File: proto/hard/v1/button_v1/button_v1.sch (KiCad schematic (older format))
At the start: 68 parts, among them J1 Conn_01x06_Female, J10 Conn_01x01_Female, J11 Conn_01x01_Female, J12 Conn_01x01_Female, J13 Conn_01x01_Female, J14 K3-2235D, J15 Conn_01x03_Male, J16 Conn_01x01_Male, J2 Conn_01x06_Female, J3 Conn_01x06_Female, J4 Conn_01x06_Female, J7 Conn_01x04_Female, J9 Conn_01x01_Female, Q1 TP0610T, Q3 TP0610T, Q6 UMG8N, Q7 UMG8N, Q8 IRLML2803, U1 LCD_2.8_SPI, U11 TC305, U12 LCD_1_8_SPI, U13 74HC595, U2 STM32F103C8Tx, U6 LM339, Y1 8MHz

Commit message: Finished main board PCB
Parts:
- removed J10, J11, J12, J13, J9: Conn_01x01_Female, Connector_Pin:Pin_D0.7mm_L6.5mm_W1.8mm_FlatFork, symbol Connector:Conn_01x01_Female
- removed J15: Conn_01x03_Male, Connector_PinHeader_2.54mm:PinHeader_1x03_P2.54mm_Vertical, symbol Connector:Conn_01x03_Male
- removed J16: Conn_01x01_Male, Connector_Pin:Pin_D0.7mm_L6.5mm_W1.8mm_FlatFork, symbol Connector:Conn_01x01_Male
- removed R35, R36, R37, R38: 3k, Resistor_SMD:R_0805_2012Metric_Pad1.15x1.40mm_HandSolder, symbol Device:R
- added J10: Conn_01x04_Male, Connector_PinHeader_2.54mm:PinHeader_1x04_P2.54mm_Vertical, symbol Connector:Conn_01x04_Male
- added J9: Conn_01x06_Male, brbuttonsystem:A1501WR-S-5P, symbol Connector:Conn_01x06_Male
- added R15: 47k, Resistor_SMD:R_0805_2012Metric_Pad1.15x1.40mm_HandSolder, symbol Device:R
- added RN2: 3k, Resistor_SMD:R_Array_Convex_4x0603, symbol Device:R_Pack04
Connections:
- net +3V3: now also R15.1
- net CX0: now also J9.1 (Pin_1)
- net CX1: now also J9.2 (Pin_2), RN2.4 (R4.1)
- net CX2: now also J9.3 (Pin_3), RN2.3 (R3.1)
- net CX3: now also J9.4 (Pin_4), RN2.2 (R2.1)
- net CX4: now also J9.5 (Pin_5), RN2.1 (R1.1)
- net EXTRA_TICK: now also U2.10 (PA0); no longer U2.41 (PB5)
- net GND: now also J10.2 (Pin_2), J9.6 (Pin_6)
- net LCD_CS: now also U2.3 (PC14); no longer U2.10 (PA0)
- net LCD_RESET: now also U12.2 (RESET)
- net MainLcdLed: now also Q8.1 (G), R12.2
- net NRST: now also J10.4 (Pin_4)
- net SWCLK: now also J10.1 (Pin_1)
- net SWDIO: now also J10.3 (Pin_3)
- net USB_PULLUP: now reaches U2.38 (PA15)
- net BACK_LCD_CS: now reaches U2.4 (PC15)
- net BACK_LCD_CS: now also U12.3 (CS)
- net at U11.5 (CX1): now also RN2.5 (R4.2)
- net at U11.6 (CX2): now also RN2.6 (R3.2)
- net at U11.7 (CX3): now also RN2.7 (R2.2)
- net at U11.8 (CX4): now also RN2.8 (R1.2)
- net at J14.3: now also R15.2
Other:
- note added: "MainLcdLed is used\nas a switch for front LCD\nand as a signal invertor\nfor back LCD switch."
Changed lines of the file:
@@
 	10100 5100 10100 5150
-$Comp
-L brbuttonsystem:LCD_2.8_SPI U1
-U 1 1 5D0C6ED3
-P 6100 850
-F 0 "U1" H 6150 900 50  0000 C CNN
-F 1 "LCD_2.8_SPI" H 6650 900 50  0000 C CNN
-F 2 "brbuttonsystem:LCD_2.8_SPI" H 6100 850 50  0001 C CNN
-F 3 "" H 6100 850 50  0001 C CNN
-	1    6100 850
-	1    0    0    -1
-$EndComp
 $Comp
 L power:+3.3V #PWR040
@@
 	0    1    -1   0
 $EndComp
-Text Label 3150 4100 0    50   ~ 0
+Text Label 1850 3800 2    50   ~ 0
 LCD_CS
 Text Label 3150 4200 0    50   ~ 0
@@
 Text Label 8800 2800 0    50   ~ 0
 CX0
-$Comp
-L Connector:Conn_01x01_Female J13
-U 1 1 5D40A8AD
-P 8600 3200
-F 0 "J13" H 8650 3200 50  0000 C CNN
-F 1 "Conn_01x01_Female" H 8492 3066 50  0001 C CNN
-F 2 "Connector_Pin:Pin_D0.7mm_L6.5mm_W1.8mm_FlatFork" H 8600 3200 50  0001 C CNN
-F 3 "~" H 8600 3200 50  0001 C CNN
-	1    8600 3200
-	-1   0    0    1
-$EndComp
-$Comp
-L Connector:Conn_01x01_Female J12
-U 1 1 5D40A741
-P 8600 3100
-F 0 "J12" H 8650 3100 50  0000 C CNN
-F 1 "Conn_01x01_Female" H 8492 2966 50  0001 C CNN
-F 2 "Connector_Pin:Pin_D0.7mm_L6.5mm_W1.8mm_FlatFork" H 8600 3100 50  0001 C CNN
-F 3 "~" H 8600 3100 50  0001 C CNN
-	1    8600 3100
-	-1   0    0    1
-$EndComp
-$Comp
-L Connector:Conn_01x01_Female J11
-U 1 1 5D40A51B
-P 8600 3000
-F 0 "J11" H 8650 3000 50  0000 C CNN
-F 1 "Conn_01x01_Female" H 8492 2866 50  0001 C CNN
-F 2 "Connector_Pin:Pin_D0.7mm_L6.5mm_W1.8mm_FlatFork" H 8600 3000 50  0001 C CNN
-F 3 "~" H 8600 3000 50  0001 C CNN
-	1    8600 3000
-	-1   0    0    1
-$EndComp
-$Comp
-L Connector:Conn_01x01_Female J10
-U 1 1 5D40A29C
-P 8600 2900
-F 0 "J10" H 8650 2900 50  0000 C CNN
-F 1 "Conn_01x01_Female" H 8492 2766 50  0001 C CNN
-F 2 "Connector_Pin:Pin_D0.7mm_L6.5mm_W1.8mm_FlatFork" H 8600 2900 50  0001 C CNN
-F 3 "~" H 8600 2900 50  0001 C CNN
-	1    8600 2900
-	-1   0    0    1
-$EndComp
 Wire Wire Line
 	9400 2300 9400 2500
-$Comp
-L power:GND #PWR0119
-U 1 1 5D50F518
-P 8950 2300
-F 0 "#PWR0119" H 8950 2050 50  0001 C CNN
-F 1 "GND" H 8955 2127 50  0001 C CNN
-F 2 "" H 8950 2300 50  0001 C CNN
-F 3 "" H 8950 2300 50  0001 C CNN
-	1    8950 2300
-	-1   0    0    1
-$EndComp
 $Comp
 L power:GND #PWR0118
@@
 $EndComp
 Wire Wire Line
-	9000 3200 8800 3200
-Wire Wire Line
-	8800 3100 9000 3100
-Wire Wire Line
-	9000 3000 8800 3000
-Wire Wire Line
-	8800 2900 9000 2900
-Wire Wire Line
 	9000 2800 8800 2800
-$Comp
-L Connector:Conn_01x01_Female J9
-U 1 1 5D47DCF2
-P 8600 2800
-F 0 "J9" H 8650 2800 50  0000 C CNN
-F 1 "Conn_01x01_Female" H 8492 2666 50  0001 C CNN
-F 2 "Connector_Pin:Pin_D0.7mm_L6.5mm_W1.8mm_FlatFork" H 8600 2800 50  0001 C CNN
-F 3 "~" H 8600 2800 50  0001 C CNN
-	1    8600 2800
-	-1   0    0    1
-$EndComp
-Wire Wire Line
-	9300 2900 9400 2900
-Wire Wire Line
-	9400 3000 9300 3000
-Wire Wire Line
-	9300 3100 9400 3100
-Wire Wire Line
-	9400 3200 9300 3200
-$Comp
-L Device:R R38
-U 1 1 5D43D79E
-P 9150 3200
-F 0 "R38" V 9200 3050 50  0000 C CNN
-F 1 "3k" V 9100 3000 50  0000 C CNN
-F 2 "Resistor_SMD:R_0805_2012Metric_Pad1.15x1.40mm_HandSolder" V 9080 3200 50  0001 C CNN
-F 3 "~" H 9150 3200 50  0001 C CNN
-	1    9150 3200
-	0    1    -1   0
-$EndComp
-$Comp
-L Device:R R37
-U 1 1 5D43D559
-P 9150 3100
-F 0 "R37" V 9200 3250 50  0000 C CNN
-F 1 "3k" V 9100 3250 50  0000 C CNN
-F 2 "Resistor_SMD:R_0805_2012Metric_Pad1.15x1.40mm_HandSolder" V 9080 3100 50  0001 C CNN
-F 3 "~" H 9150 3100 50  0001 C CNN
-	1    9150 3100
-	0    1    -1   0
-$EndComp
-$Comp
-L Device:R R36
-U 1 1 5D43C594
-P 9150 3000
-F 0 "R36" V 9200 2850 50  0000 C CNN
-F 1 "3k" V 9100 2800 50  0000 C CNN
-F 2 "Resistor_SMD:R_0805_2012Metric_Pad1.15x1.40mm_HandSolder" V 9080 3000 50  0001 C CNN
-F 3 "~" H 9150 3000 50  0001 C CNN
-	1    9150 3000
-	0    1    -1   0
-$EndComp
-$Comp
-L Device:R R35
-U 1 1 5D43C3D6
-P 9150 2900
-F 0 "R35" V 9200 3050 50  0000 C CNN
-F 1 "3k" V 9100 3050 50  0000 C CNN
-F 2 "Resistor_SMD:R_0805_2012Metric_Pad1.15x1.40mm_HandSolder" V 9080 2900 50  0001 C CNN
-F 3 "~" H 9150 2900 50  0001 C CNN
-	1    9150 2900
-	0    1    -1   0
-$EndComp
+Wire Wire Line
+	9350 2900 9400 2900
+Wire Wire Line
+	9400 3000 9350 3000
+Wire Wire Line
+	9350 3100 9400 3100
+Wire Wire Line
+	9400 3200 9350 3200
 Wire Wire Line
 	9300 2800 9400 2800
@@
 $EndComp
 $Sheet
-S 2250 750  500  750
+S 1150 1450 500  750
 U 5D3754B9
 F0 "Entertainment" 50
 F1 "Entertainment.sch" 50
-F2 "EXT_READ" I L 2250 850 50
-F3 "EXT_RW" I L 2250 950 50
-F4 "EXT_WRITE" I L 2250 1050 50
-F5 "StartLed" I L 2250 1200 50
-F6 "Sound_PWM" I L 2250 1300 50
-F7 "BuzzerEnable" I L 2250 1400 50
+F2 "EXT_READ" I L 1150 1550 50
+F3 "EXT_RW" I L 1150 1650 50
+F4 "EXT_WRITE" I L 1150 1750 50
+F5 "StartLed" I L 1150 1900 50
+F6 "Sound_PWM" I L 1150 2000 50
+F7 "BuzzerEnable" I L 1150 2100 50
 $EndSheet
-Text Label 2150 850  2    50   ~ 0
+Text Label 1050 1550 2    50   ~ 0
 EXT_READ
-Text Label 2150 950  2    50   ~ 0
+Text Label 1050 1650 2    50   ~ 0
 EXT_RW
-Text Label 2150 1050 2    50   ~ 0
+Text Label 1050 1750 2    50   ~ 0
 EXT_WRITE
-Text Label 2150 1200 2    50   ~ 0
+Text Label 1050 1900 2    50   ~ 0
 StartLed
-Text Label 2150 1300 2    50   ~ 0
+Text Label 1050 2000 2    50   ~ 0
 Sound_PWM
 Wire Wire Line
-	2250 1300 2150 1300
-Wire Wire Line
-	2150 1200 2250 1200
-Wire Wire Line
-	2250 1050 2150 1050
-Wire Wire Line
-	2150 950  2250 950
-Wire Wire Line
-	2250 850  2150 850
+	1150 2000 1050 2000
+Wire Wire Line
+	1050 1900 1150 1900
+Wire Wire Line
+	1150 1750 1050 1750
+Wire Wire Line
+	1050 1650 1150 1650
+Wire Wire Line
+	1150 1550 1050 1550
 Text GLabel 3400 5300 2    50   Input ~ 0
 D+
@@
 D-
 $Sheet
-S 750  750  550  500
+S 1150 700  550  500
 U 5D4A520B
 F0 "PowerInput" 50
 F1 "PowerInput.sch" 50
+F2 "USB_PULLUP" I L 1150 800 50
 $EndSheet
 Connection ~ 3450 900
@@
 Text Label 5000 3800 2    50   ~ 0
 EXTRA_TICK
-Text Label 1850 4600 2    50   ~ 0
+Text Label 3150 4100 0    50   ~ 0
 EXTRA_TICK
 $Comp
@@
 	1    0    0    -1
 $EndComp
-Text Label 2150 1400 2    50   ~ 0
+Text Label 1050 2100 2    50   ~ 0
 BuzzerEnable
 Wire Wire Line
-	2150 1400 2250 1400
+	1050 2100 1150 2100
 Wire Wire Line
 	7200 3600 7300 3600
@@
 	1    0    0    -1
 $EndComp
-$Comp
-L Connector:Conn_01x03_Male J15
-U 1 1 5D4C3FA1
-P 1850 6600
-F 0 "J15" H 1958 6789 50  0000 C CNN
-F 1 "Conn_01x03_Male" H 1958 6790 50  0001 C CNN
-F 2 "Connector_PinHeader_2.54mm:PinHeader_1x03_P2.54mm_Vertical" H 1850 6600 50  0001 C CNN
-F 3 "~" H 1850 6600 50  0001 C CNN
-	1    1850 6600
-	1    0    0    -1
-$EndComp
-$Comp
-L Connector:Conn_01x01_Male J16
-U 1 1 5D4C52F9
-P 1850 7000
-F 0 "J16" H 1958 7089 50  0000 C CNN
-F 1 "Conn_01x01_Male" H 1958 7090 50  0001 C CNN
-F 2 "Connector_Pin:Pin_D0.7mm_L6.5mm_W1.8mm_FlatFork" H 1850 7000 50  0001 C CNN
-F 3 "~" H 1850 7000 50  0001 C CNN
-	1    1850 7000
-	1    0    0    -1
-$EndComp
-Text Label 2050 7000 0    50   ~ 0
+Text Label 2050 6800 0    50   ~ 0
 NRST
 Text Label 2050 6500 0    50   ~ 0
@@
 	0    -1   -1   0
 $EndComp
+Text Label 4850 6750 2    50   ~ 0
+BACK_LCD_CS
+$Comp
+L brbuttonsystem:LCD_2.8_SPI U1
+U 1 1 5D0C6ED3
+P 6100 850
+F 0 "U1" H 6150 900 50  0000 C CNN
+F 1 "LCD_2.8_SPI" H 6650 900 50  0000 C CNN
+F 2 "brbuttonsystem:LCD_2.8_SPI" H 6100 850 50  0001 C CNN
+F 3 "" H 6100 850 50  0001 C CNN
+	1    6100 850
+	1    0    0    -1
+$EndComp
+Text Label 4850 6650 2    50   ~ 0
+LCD_RESET
+$Comp
+L Connector:Conn_01x06_Male J9
+U 1 1 5D728F35
+P 8600 3000
+F 0 "J9" H 8573 2928 50  0000 R CNN
+F 1 "Conn_01x06_Male" H 8708 3290 50  0001 C CNN
+F 2 "brbuttonsystem:A1501WR-S-5P" H 8600 3000 50  0001 C CNN
+F 3 "~" H 8600 3000 50  0001 C CNN
+	1    8600 3000
+	1    0    0    -1
+$EndComp
+$Comp
+L power:GND #PWR0119
+U 1 1 5D50F518
+P 8950 2300
+F 0 "#PWR0119" H 8950 2050 50  0001 C CNN
+F 1 "GND" H 8955 2127 50  0001 C CNN
+F 2 "" H 8950 2300 50  0001 C CNN
+F 3 "" H 8950 2300 50  0001 C CNN
+	1    8950 2300
+	-1   0    0    1
+$EndComp
+$Comp
+L power:GND #PWR0145
+U 1 1 5D73EE93
+P 8800 3300
+F 0 "#PWR0145" H 8800 3050 50  0001 C CNN
+F 1 "GND" H 8805 3127 50  0001 C CNN
+F 2 "" H 8800 3300 50  0001 C CNN
+F 3 "" H 8800 3300 50  0001 C CNN
+	1    8800 3300
+	1    0    0    -1
+$EndComp
+Text Label 1850 3900 2    50   ~ 0
+BACK_LCD_CS
+Text Label 4300 6350 2    50   ~ 0
+MainLcdLed
+Text Notes 4550 1950 0    50   ~ 0
+MainLcdLed is used\nas a switch for front LCD\nand as a signal invertor\nfor back LCD switch.
+Text Label 3150 5600 0    50   ~ 0
+USB_PULLUP
+$Comp
+L Device:R_Pack04 RN2
+U 1 1 5D6AA8DC
+P 9150 3000
+F 0 "RN2" V 8850 3100 50  0000 C CNN
+F 1 "3k" V 8850 2950 50  0000 C CNN
+F 2 "Resistor_SMD:R_Array_Convex_4x0603" V 9425 3000 50  0001 C CNN
+F 3 "~" H 9150 3000 50  0001 C CNN
+	1    9150 3000
+	0    1    -1   0
+$EndComp
+Wire Wire Line
+	8950 2900 8800 2900
+Wire Wire Line
+	8800 3000 8950 3000
+Wire Wire Line
+	8950 3100 8800 3100
+Wire Wire Line
+	8800 3200 8950 3200
+Text Label 1050 800  2    50   ~ 0
+USB_PULLUP
+Wire Wire Line
+	1050 800  1150 800
+$Comp
+L Device:R R15
+U 1 1 5D6C1AC9
+P 8250 2400
+F 0 "R15" V 8350 2300 50  0000 C CNN
+F 1 "47k" V 8350 2450 50  0000 C CNN
+F 2 "Resistor_SMD:R_0805_2012Metric_Pad1.15x1.40mm_HandSolder" V 8180 2400 50  0001 C CNN
+F 3 "~" H 8250 2400 50  0001 C CNN
+	1    8250 2400
+	0    1    1    0
+$EndComp
+$Comp
+L power:+3.3V #PWR0146
+U 1 1 5D6C3AA5
+P 8400 2400
+F 0 "#PWR0146" H 8400 2250 50  0001 C CNN
+F 1 "+3.3V" V 8300 2450 50  0000 C CNN
+F 2 "" H 8400 2400 50  0001 C CNN
+F 3 "" H 8400 2400 50  0001 C CNN
+	1    8400 2400
+	0    1    1    0
+$EndComp
+$Comp
+L Connector:Conn_01x04_Male J10
+U 1 1 5D6C6312
+P 1850 6600
+F 0 "J10" H 1958 6789 50  0000 C CNN
+F 1 "Conn_01x04_Male" H 1958 6790 50  0001 C CNN
+F 2 "Connector_PinHeader_2.54mm:PinHeader_1x04_P2.54mm_Vertical" H 1850 6600 50  0001 C CNN
+F 3 "~" H 1850 6600 50  0001 C CNN
+	1    1850 6600
+	1    0    0    -1
+$EndComp
 $EndSCHEMATC

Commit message: Finised and reviewed v2 of main board. Schematic pdf, BOM and gerber archive are updated.
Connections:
- net EXTRA_TICK renamed BACK_LED_CS
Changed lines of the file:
@@
 Text Label 3150 5100 0    50   ~ 0
 EXT_RW
-Text Label 1150 5000 2    50   ~ 0
-DISP_SDA
-Text Label 1150 4900 2    50   ~ 0
-DISP_SCL
 Text Label 1850 4800 2    50   ~ 0
 EXT_READ
@@
 Text Label 1850 3700 2    50   ~ 0
 TouchEnable
-Text Label 1150 3800 2    50   ~ 0
-Touch4Front
 $Comp
 L power:GND #PWR036
@@
 LCD_MOSI
 Text Label 5000 3800 2    50   ~ 0
-EXTRA_TICK
+BACK_LED_CS
 Text Label 3150 4100 0    50   ~ 0
-EXTRA_TICK
+BACK_LED_CS
 $Comp
 L brbuttonsystem:UMG8N Q6
@@
 	1    0    0    -1
 $EndComp
-Text Label 1150 4500 2    50   ~ 0
-BuzzerEnable
 Wire Wire Line
 	9600 5050 9650 5050

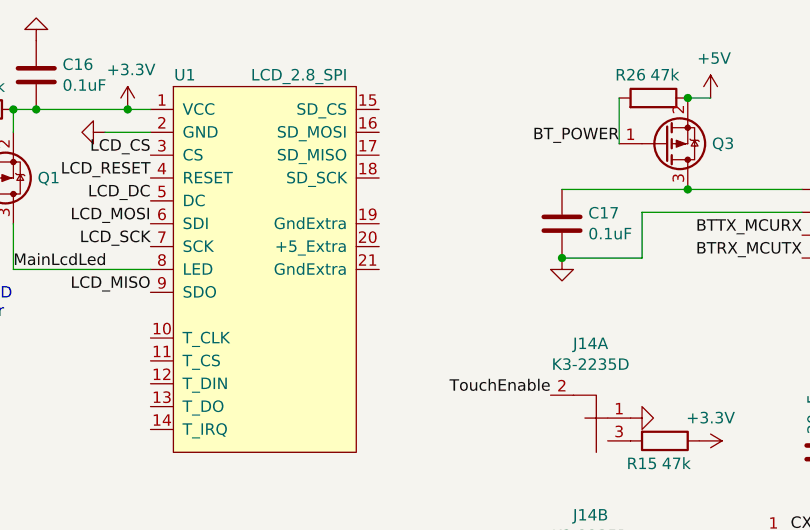
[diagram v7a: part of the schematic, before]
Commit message: Updated main board to v0.3: - changed power coils to bobbin - added test point for StartLED line - integrated new LCD screen footprint with LED power connectors - changed Schottky diode footprint to smaller in start LED converter - changed crystal footprint to smaller - added guard ring around crystal - disconnected USB shield from GND line
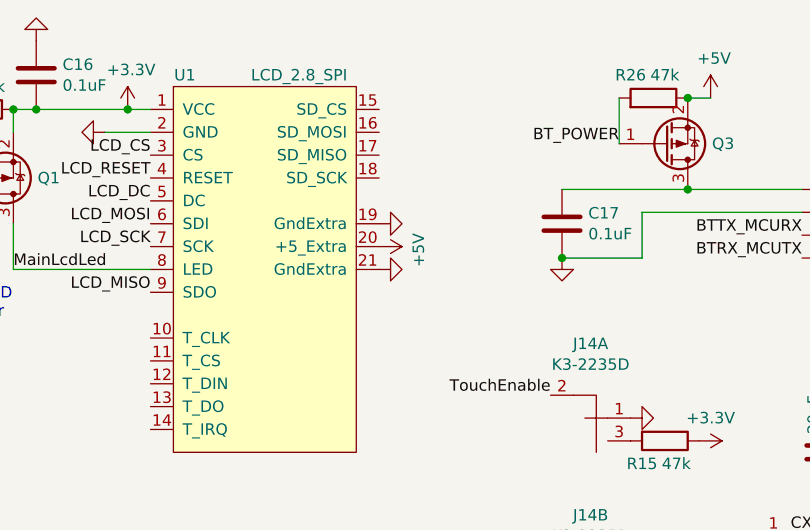
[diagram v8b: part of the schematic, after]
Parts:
- Y1: footprint Crystal:Crystal_SMD_5032-2Pin_5.0x3.2mm_HandSoldering -> Crystal:Crystal_SMD_5032-2Pin_5.0x3.2mm
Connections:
- net +5V: now also U1.20 (+5_Extra)
- net GND: now also U1.19 (GndExtra), U1.21 (GndExtra)
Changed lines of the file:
@@
 F 0 "Y1" H 2950 6650 50  0000 C CNN
 F 1 "8MHz" H 3150 6650 50  0000 C CNN
-F 2 "Crystal:Crystal_SMD_5032-2Pin_5.0x3.2mm_HandSoldering" H 3050 6500 50  0001 C CNN
+F 2 "Crystal:Crystal_SMD_5032-2Pin_5.0x3.2mm" H 3050 6500 50  0001 C CNN
 F 3 "~" H 3050 6500 50  0001 C CNN
 	1    3050 6500
@@
 	1    0    0    -1
 $EndComp
+$Comp
+L power:GND #PWR0147
+U 1 1 5EBC5070
+P 7000 1450
+F 0 "#PWR0147" H 7000 1200 50  0001 C CNN
+F 1 "GND" H 7005 1277 50  0001 C CNN
+F 2 "" H 7000 1450 50  0001 C CNN
+F 3 "" H 7000 1450 50  0001 C CNN
+	1    7000 1450
+	0    -1   -1   0
+$EndComp
+$Comp
+L power:GND #PWR0148
+U 1 1 5EBC55DD
+P 7000 1650
+F 0 "#PWR0148" H 7000 1400 50  0001 C CNN
+F 1 "GND" H 7005 1477 50  0001 C CNN
+F 2 "" H 7000 1650 50  0001 C CNN
+F 3 "" H 7000 1650 50  0001 C CNN
+	1    7000 1650
+	0    -1   -1   0
+$EndComp
+$Comp
+L power:+5V #PWR0149
+U 1 1 5EBC6CA1
+P 7000 1550
+F 0 "#PWR0149" H 7000 1400 50  0001 C CNN
+F 1 "+5V" H 7015 1723 50  0000 C CNN
+F 2 "" H 7000 1550 50  0001 C CNN
+F 3 "" H 7000 1550 50  0001 C CNN
+	1    7000 1550
+	0    1    1    0
+$EndComp
 $EndSCHEMATC
